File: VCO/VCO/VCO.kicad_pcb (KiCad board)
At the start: 2 copper layers, 46 x 116.5 mm, 92 parts, among them J13 Conn_02x05_Odd_Even, J15 Conn_01x06, J17 Conn_01x11, J19 Conn_01x02, Q1 SSM2210, Q2 PN4391, U1 OP275, U2 TL072, U3 TL074, U4 LM13700, U5 TL072, U6 TL071

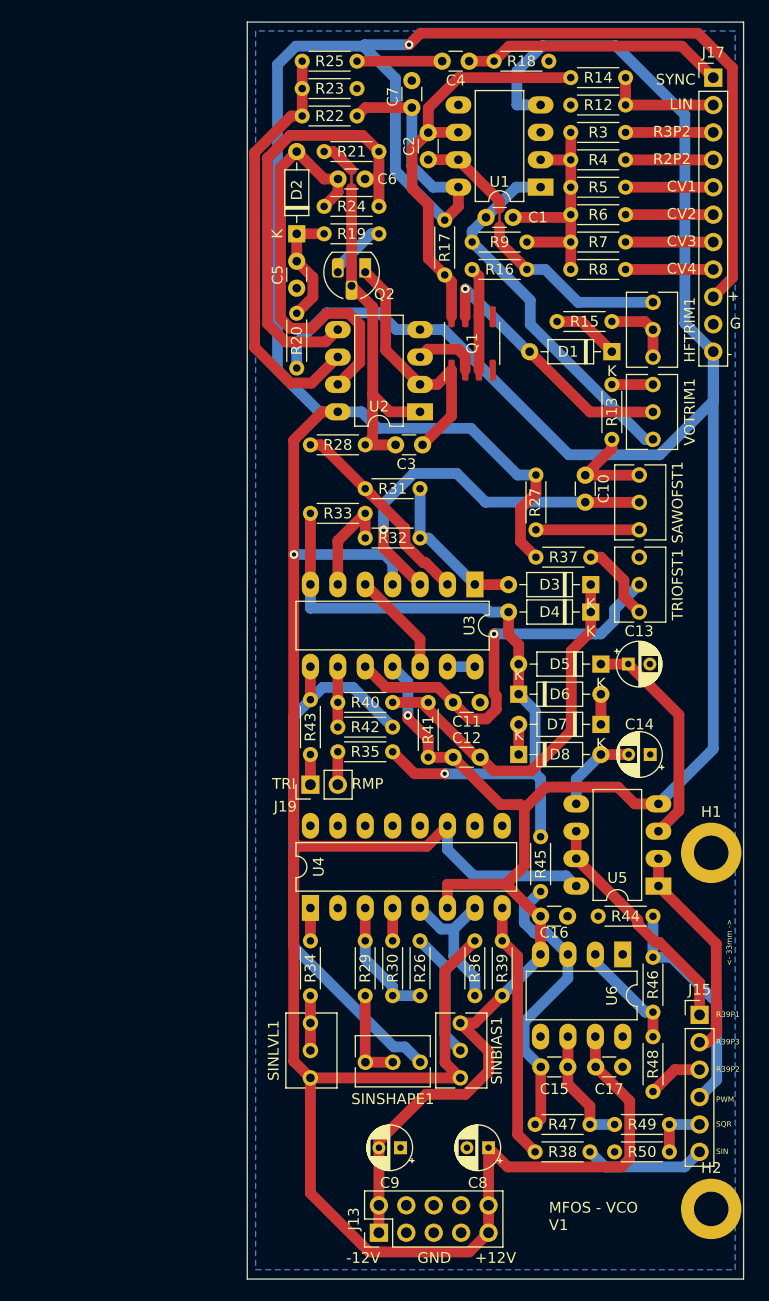
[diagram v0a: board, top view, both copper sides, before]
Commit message: VCO - changed resistors size
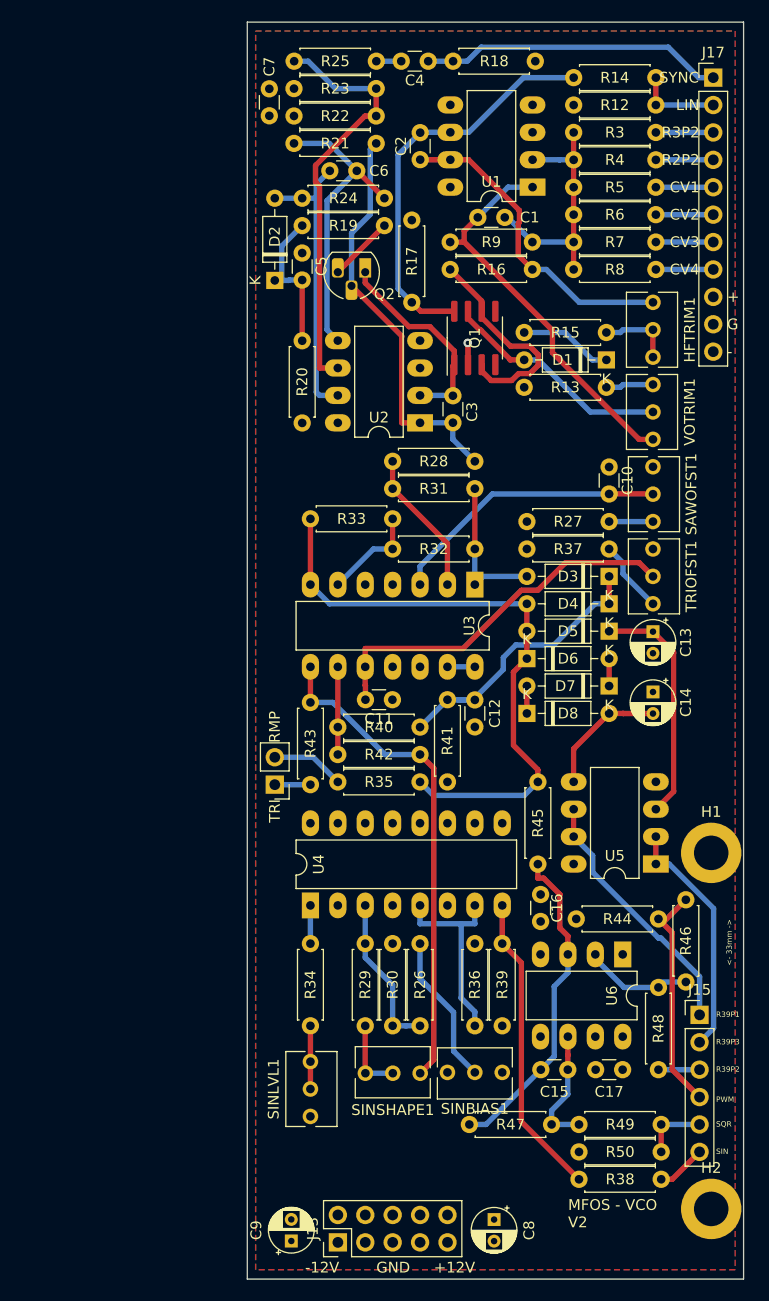
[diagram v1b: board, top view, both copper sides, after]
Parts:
- R12, R13, R14, R15, R16, R17, R18, R19, R20, R21, R22, R23, R24, R25, R26, R27, R28, R29, R3, R30, R31, R32, R33, R34, R35, R36, R37, R38, R39, R4, R40, R41, R42, R43, R44, R45, R46, R47, R48, R49, R5, R50, R6, R7, R8, R9: footprint Resistor_THT:R_Axial_DIN0204_L3.6mm_D1.6mm_P5.08mm_Horizontal -> Library:R_Axial_DIN0207_L6.3mm_D2.5mm_P7.62mm_Horizontal
- moved C9 13.3 mm to (84.1, 133.0), turned to 90 degrees
- moved C7 13.2 mm to (82.0, 26.2)
- moved R28 10.3 mm to (101.1, 60.7)
- moved R13 9.45 mm to (105.7, 53.8), turned to 0 degrees
- moved C11 8.13 mm to (93.5, 82.8)
- moved R22 6.86 mm to (91.9, 28.7), turned to 180 degrees
- moved R23 6.86 mm to (91.9, 26.2), turned to 180 degrees
- moved R27 6.83 mm to (113.5, 66.3), turned to 180 degrees
- moved C8 6.67 mm to (102.9, 131.0), turned to -90 degrees
- moved R46 6.14 mm to (120.7, 101.3)
- moved R47 6.10 mm to (100.6, 122.2)
- moved SINBIAS1 6.00 mm to (103.6, 117.3), turned to 0 degrees
- moved C14 5.80 mm to (117.6, 82.1), turned to -90 degrees
- moved C3 5.35 mm to (99.1, 54.6), turned to -90 degrees
- moved R20 5.11 mm to (85.1, 57.2)
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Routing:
- net +12V: track 370.7 -> 0.00 mm, vias 2 -> 0
- net -12V: track 241.0 -> 0.00 mm, vias 1 -> 0
- net GND: track 28.2 -> 2.03 mm, vias 0 -> 1
- net Net-(U2B-+): track 41.2 -> 27.8 mm
- net Net-(D2-A): track 39.2 -> 27.0 mm
- net Net-(Q1A-E1): track 9.60 -> 20.1 mm
- net Net-(D3-K): track 35.9 -> 27.0 mm
- net Net-(U3A-+): track 34.9 -> 26.1 mm, vias 1 -> 0
- net SIN: track 11.3 -> 4.61 mm
- net Net-(D4-A): track 63.5 -> 56.8 mm, vias 1 -> 0
- net Net-(R42-Pad2): track 52.4 -> 46.0 mm
- net Net-(U3A--): track 19.6 -> 13.5 mm
- net Net-(C4-Pad2): track 7.89 -> 2.31 mm
- net Net-(R27-Pad1): track 9.58 -> 4.06 mm
- net Net-(Q1A-C1): track 24.0 -> 19.1 mm
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- added copper zone on F.Cu, net +12V
- added copper zone on B.Cu, net -12V
- added copper zone on In1.Cu, net GND
- added copper zone on In2.Cu, net GND
- removed copper zone on B.Cu, net GND
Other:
- copper layers 2 -> 4
- board text added: "MFOS - VCO V2"
- board text removed: "MFOS - VCO V1"

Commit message: VCO - fixes
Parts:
- added R51: 130K, Library:R_Axial_DIN0207_L6.3mm_D2.5mm_P7.62mm_Horizontal, F.Cu at (59.9, 105.5)
- C11: value 100pF -> 100nF
- C3: footprint Capacitor_THT:C_Disc_D3.0mm_W1.6mm_P2.50mm -> Capacitor_THT:C_Radial_D5.0mm_H11.0mm_P2.00mm
- C4: value npF -> 1nF
- HFTRIM1, SAWOFST1, SINBIAS1, SINLVL1, SINSHAPE1, TRIOFST1, VOTRIM1: footprint Potentiometer_THT:Potentiometer_Bourns_3266Y_Vertical -> Potentiometer_THT:Potentiometer_Bourns_3296W_Vertical

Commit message: VCO - fixes
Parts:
- moved R51 39.4 mm to (98.6, 113.0), turned to 90 degrees
- moved C10 12.8 mm to (103.4, 69.1), turned to 90 degrees
- moved SAWOFST1 11.5 mm to (106.2, 60.7), turned to 180 degrees
- moved SINLVL1 9.54 mm to (84.3, 106.9)
- moved SINSHAPE1 7.89 mm to (83.1, 117.3)
- moved SINBIAS1 5.33 mm to (98.3, 117.3)
- moved VOTRIM1 3.30 mm to (117.6, 62.0)
- moved R34 2.54 mm to (88.4, 113.0)
- moved C3 2.10 mm to (101.1, 55.1)
- moved TRIOFST1 1.78 mm to (117.6, 67.1)
- moved HFTRIM1 0.76 mm to (117.6, 51.8)
- moved R16 0.25 mm to (98.8, 43.2)
- moved R9 0.25 mm to (106.4, 40.6)
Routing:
- net Net-(R42-Pad2): track 46.0 -> 52.8 mm
- net Net-(U3A-+): track 26.1 -> 21.3 mm
- net Net-(R29-Pad1): track 6.94 -> 10.6 mm
- net Net-(Q1A-C1): track 19.1 -> 21.9 mm
- net Net-(C1-Pad2): track 36.6 -> 39.3 mm
- net Net-(R36-Pad2): track 18.5 -> 21.0 mm
- net Net-(R27-Pad1): track 4.06 -> 6.54 mm
- net Net-(R34-Pad1): track 5.86 -> 8.08 mm
- net Net-(R13-Pad2): track 4.42 -> 6.62 mm
- net Net-(D1-A): track 21.4 -> 23.3 mm
- net Net-(R37-Pad1): track 6.76 -> 5.43 mm
- net RAW: track 37.9 -> 39.1 mm
- net Net-(R34-Pad2): track 3.54 -> 4.59 mm
- net Net-(R26-Pad1): track 14.0 -> 13.1 mm
- net Net-(Q1A-E1): track 20.1 -> 20.7 mm
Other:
- board text added: "JLCJLCJLCJLC"
- board text added: "MFOS - VCO V3"
- board text removed: "MFOS - VCO V2"

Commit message: misc
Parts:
- added TP1: TestPoint, TestPoint:TestPoint_THTPad_D1.5mm_Drill0.7mm, F.Cu at (101.1, 63.2)
- added TP2: TestPoint, TestPoint:TestPoint_THTPad_D1.5mm_Drill0.7mm, F.Cu at (82.8, 79.8)
- added TP3: TestPoint, TestPoint:TestPoint_THTPad_D1.5mm_Drill0.7mm, F.Cu at (84.8, 62.2)
- moved R9 5.39 mm to (105.7, 46.0)
- moved R28 5.08 mm to (96.0, 60.7)
- moved R31 5.08 mm to (88.4, 63.2)
- moved Q1 3.43 mm to (101.7, 45.9)
- moved R16 2.55 mm to (99.1, 40.6)
- moved R17 2.54 mm to (95.2, 43.4)
- renumbered SAWOFST1 to RMPOFST1
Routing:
- net Net-(D1-A): track 23.3 -> 38.9 mm
- net RAW: track 39.1 -> 50.7 mm
- net Net-(Q1A-E1): track 20.7 -> 10.5 mm
- net Net-(U1A--): track 24.3 -> 31.1 mm
- net Net-(D3-A): track 14.0 -> 20.5 mm
- net Net-(U3A--): track 13.5 -> 18.6 mm
- net Net-(C1-Pad2): track 39.3 -> 43.2 mm
- net Net-(R42-Pad2): track 52.8 -> 55.9 mm
- net Net-(Q1B-C2): track 37.7 -> 35.5 mm
- net Net-(Q1A-C1): track 21.9 -> 23.5 mm

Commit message: VCO cleanup board
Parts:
- moved C8 3.66 mm to (104.0, 127.5)
- moved C9 3.64 mm to (83.0, 129.5)
- moved J13 3.06 mm to (88.5, 130.0)
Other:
- board size 46 x 116.5 mm -> 46 x 113 mm
